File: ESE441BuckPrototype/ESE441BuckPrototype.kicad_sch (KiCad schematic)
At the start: 0 parts

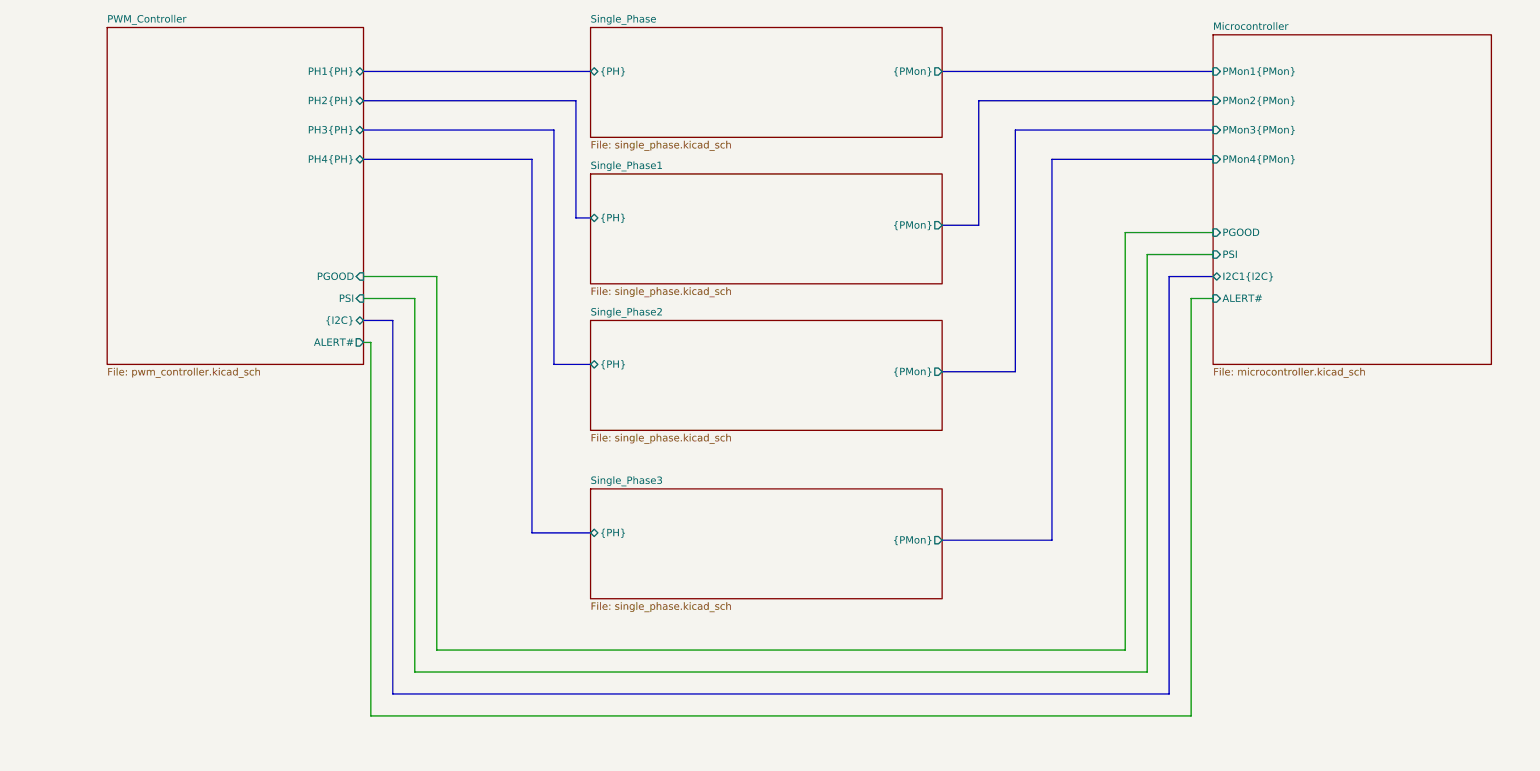
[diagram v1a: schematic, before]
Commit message: Connect enable to MCU; Testpoints
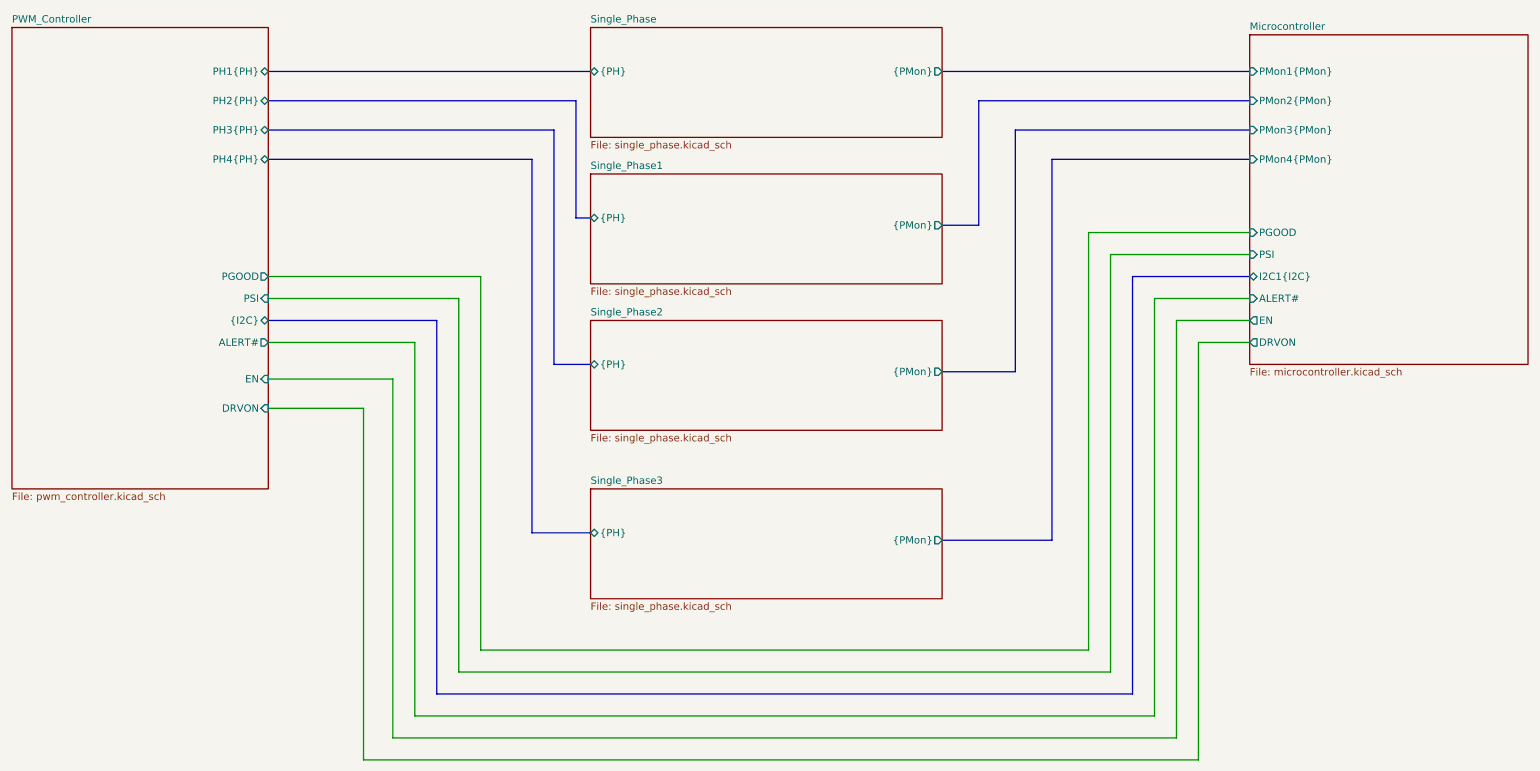
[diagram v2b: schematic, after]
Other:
- sheet Microcontroller ports: added DRVON, EN; removed none
- sheet PWM_Controller ports: added DRVON, EN; removed none
